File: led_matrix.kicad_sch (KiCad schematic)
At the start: 160 parts, among them Q1 BSS84, Q10 BSS84, Q11 2N7002, Q12 2N7002, Q13 2N7002, Q14 2N7002, Q15 2N7002, Q16 2N7002, Q17 2N7002, Q18 2N7002, Q19 2N7002, Q2 BSS84, Q20 2N7002, Q3 BSS84, Q4 BSS84, Q5 BSS84, Q6 BSS84, Q7 BSS84, Q8 BSS84, Q9 BSS84

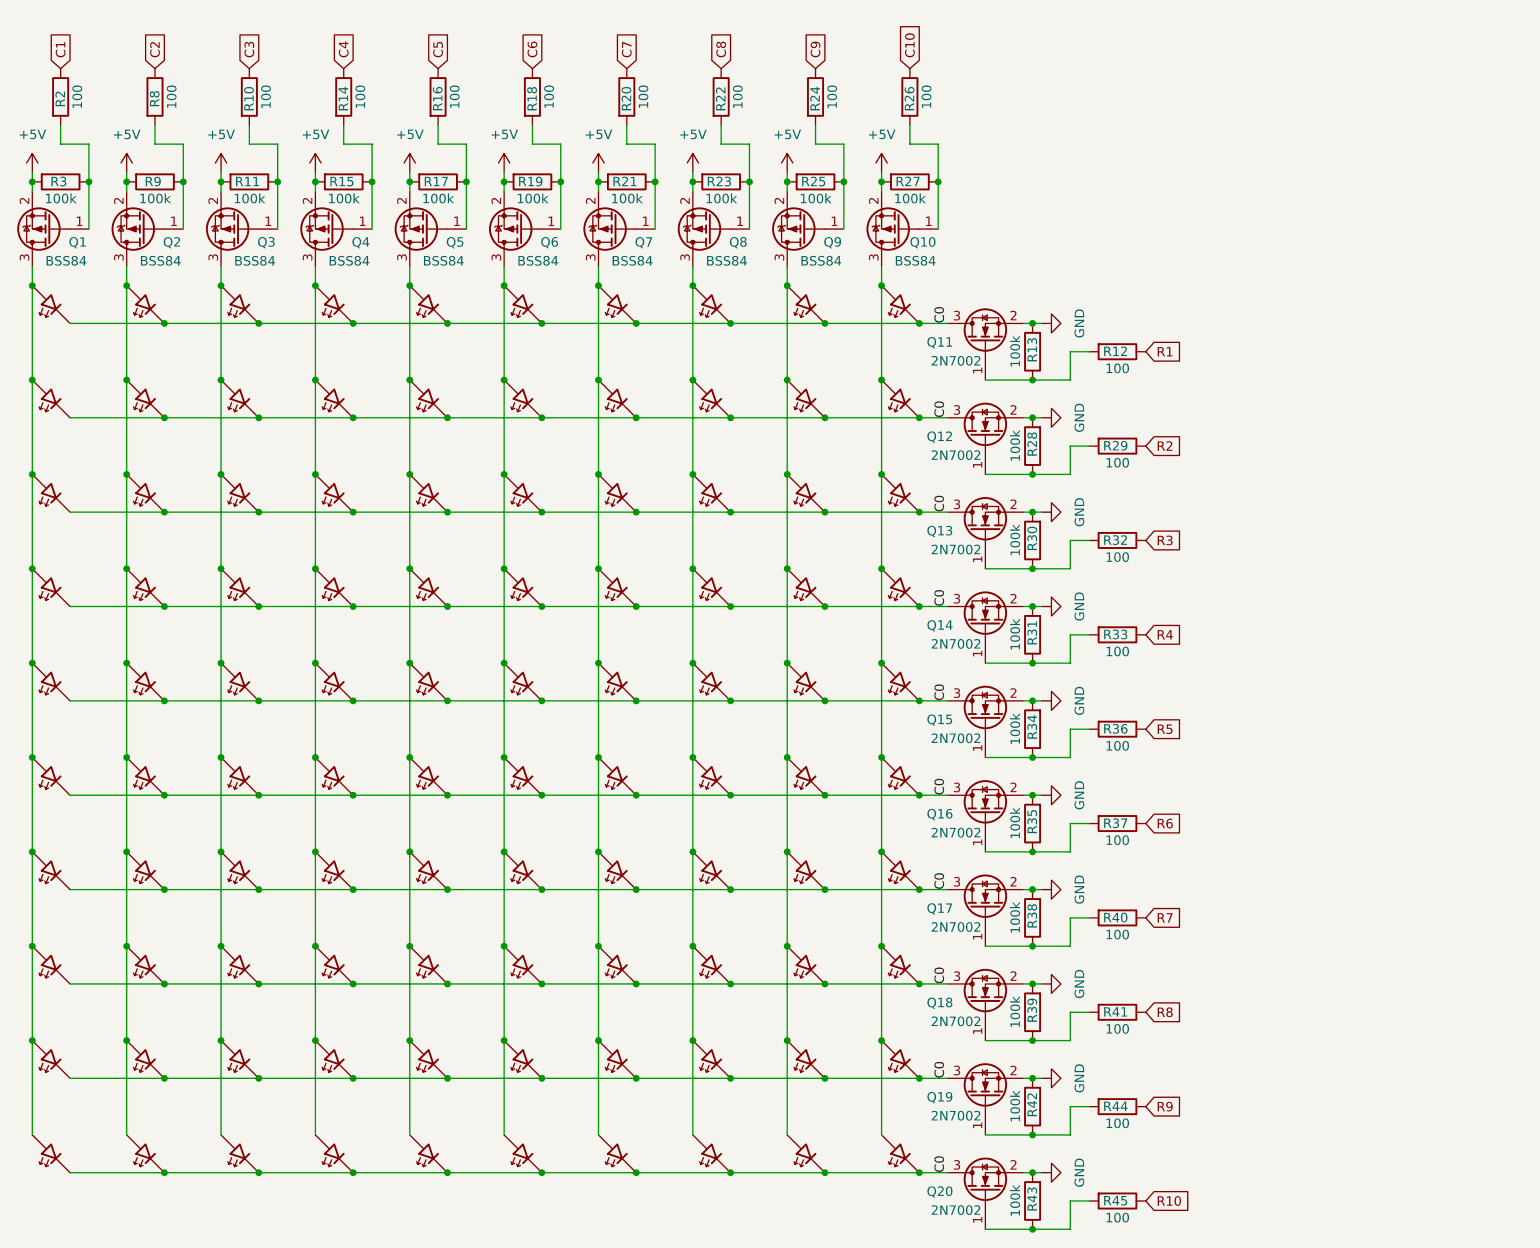
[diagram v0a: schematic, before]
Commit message: Creataed many hierarchical sheet
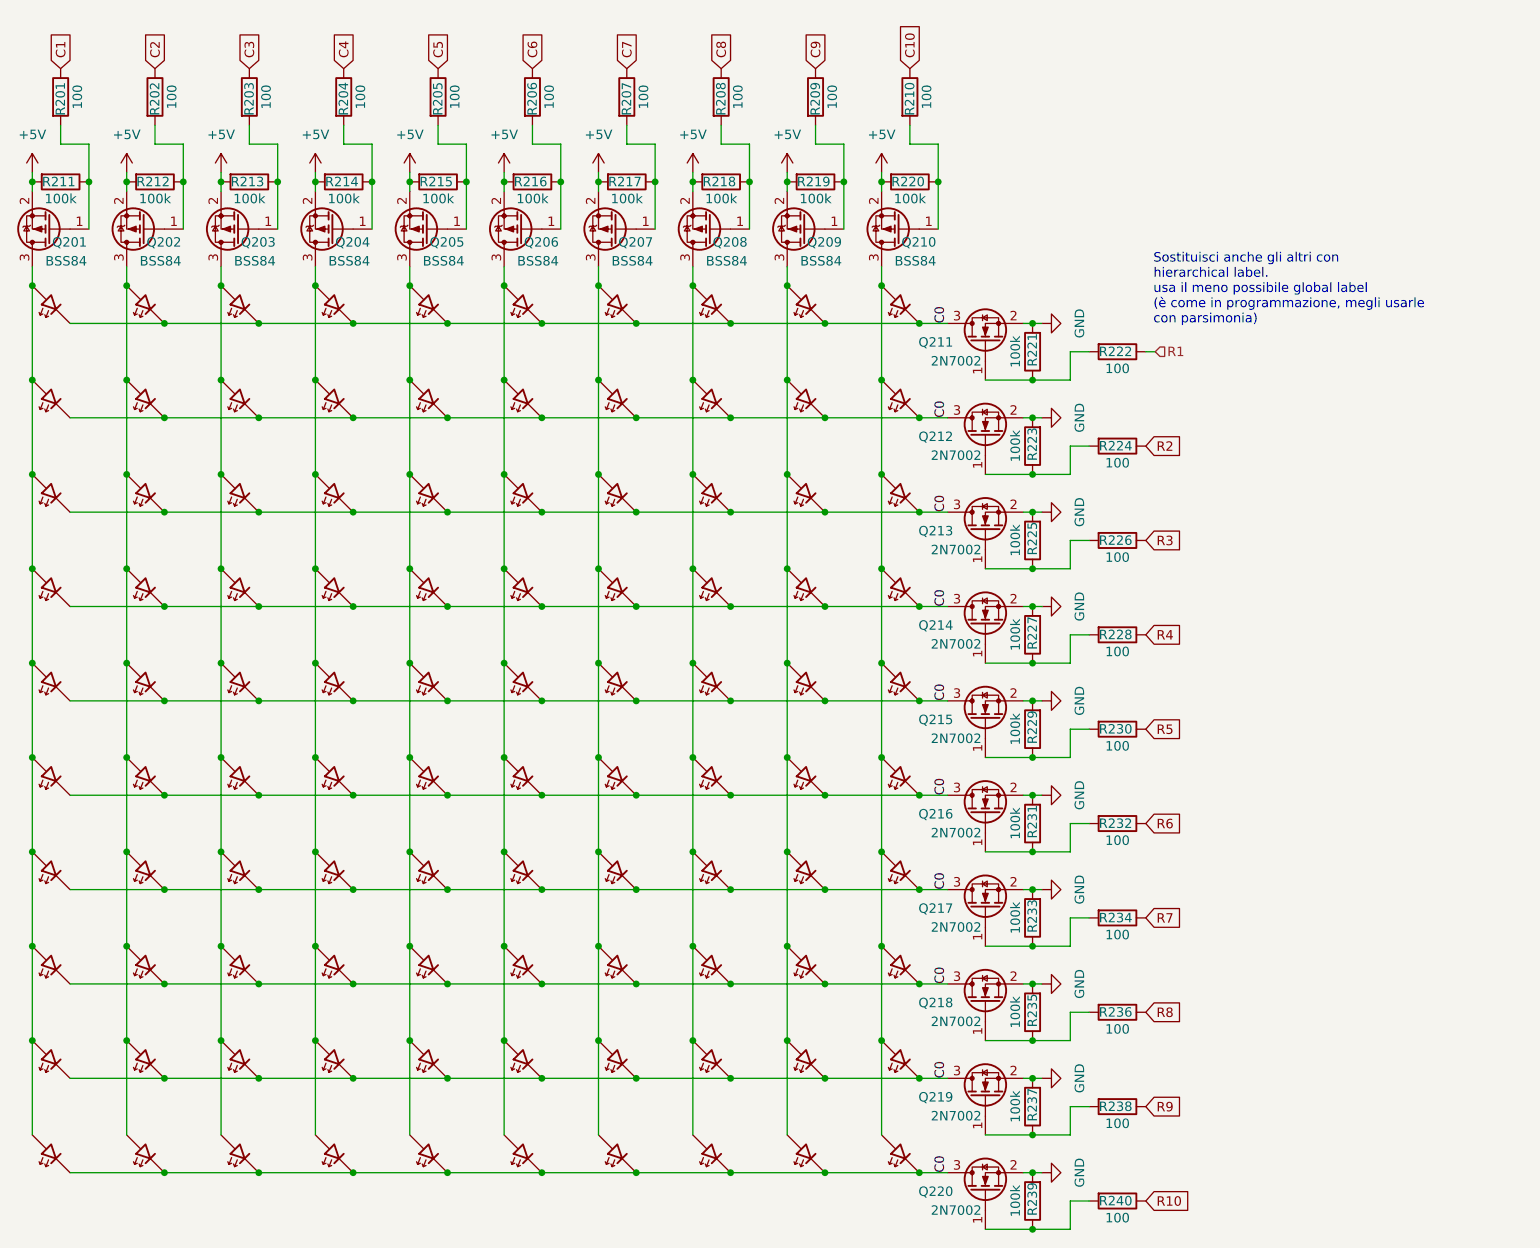
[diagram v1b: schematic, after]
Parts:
- renumbered D1 to D201, D11 to D202, D21 to D203, D31 to D204, D41 to D205, D51 to D206, D61 to D207, D71 to D208, D81 to D209, D91 to D210, D2 to D211, D12 to D212, D22 to D213, D32 to D214, D42 to D215, D52 to D216, D62 to D217, D72 to D218, D82 to D219, D92 to D220, D3 to D221, D13 to D222, D23 to D223, D33 to D224, D43 to D225, D53 to D226, D63 to D227, D73 to D228, D83 to D229, D93 to D230, D4 to D231, D14 to D232, D24 to D233, D34 to D234, D44 to D235, D54 to D236, D64 to D237, D74 to D238, D84 to D239, D94 to D240, D5 to D241, D15 to D242, D25 to D243, D35 to D244, D45 to D245, D55 to D246, D65 to D247, D75 to D248, D85 to D249, D95 to D250, D6 to D251, D16 to D252, D26 to D253, D36 to D254, D46 to D255, D56 to D256, D66 to D257, D76 to D258, D86 to D259, D96 to D260, D7 to D261, D17 to D262, D27 to D263, D37 to D264, D47 to D265, D57 to D266, D67 to D267, D77 to D268, D87 to D269, D97 to D270, D8 to D271, D18 to D272, D28 to D273, D38 to D274, D48 to D275, D58 to D276, D68 to D277, D78 to D278, D88 to D279, D98 to D280, D9 to D281, D19 to D282, D29 to D283, D39 to D284, D49 to D285, D59 to D286, D69 to D287, D79 to D288, D89 to D289, D99 to D290, D10 to D291, D20 to D292, D30 to D293, D40 to D294, D50 to D295, D60 to D296, D70 to D297, D80 to D298, D90 to D299, D100 to D300, Q1 to Q201, Q2 to Q202, Q3 to Q203, Q4 to Q204, Q5 to Q205, Q6 to Q206, Q7 to Q207, Q8 to Q208, Q9 to Q209, Q10 to Q210, Q11 to Q211, Q12 to Q212, Q13 to Q213, Q14 to Q214, Q15 to Q215, Q16 to Q216, Q17 to Q217, Q18 to Q218, Q19 to Q219, Q20 to Q220, R2 to R201, R8 to R202, R10 to R203, R14 to R204, R16 to R205, R18 to R206, R20 to R207, R22 to R208, R24 to R209, R26 to R210, R3 to R211, R9 to R212, R11 to R213, R15 to R214, R17 to R215, R19 to R216, R21 to R217, R23 to R218, R25 to R219, R27 to R220, R13 to R221, R12 to R222, R28 to R223, R29 to R224, R30 to R225, R32 to R226, R31 to R227, R33 to R228, R34 to R229, R36 to R230, R35 to R231, R37 to R232, R38 to R233, R40 to R234, R39 to R235, R41 to R236, R42 to R237, R44 to R238, R43 to R239, R45 to R240
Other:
- note added: "Sostituisci anche gli altri con hierarchical label. usa il meno possibile global label (è come in programmazione, megli usarle con parsimonia)"
